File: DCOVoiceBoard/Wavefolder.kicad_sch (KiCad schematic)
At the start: 39 parts, among them Q401 BC858, Q402 BC857, Q403 BC847, Q404 BC857, Q405 BC847, U302 TMUX4053, U402 LM13700, U403 TL074

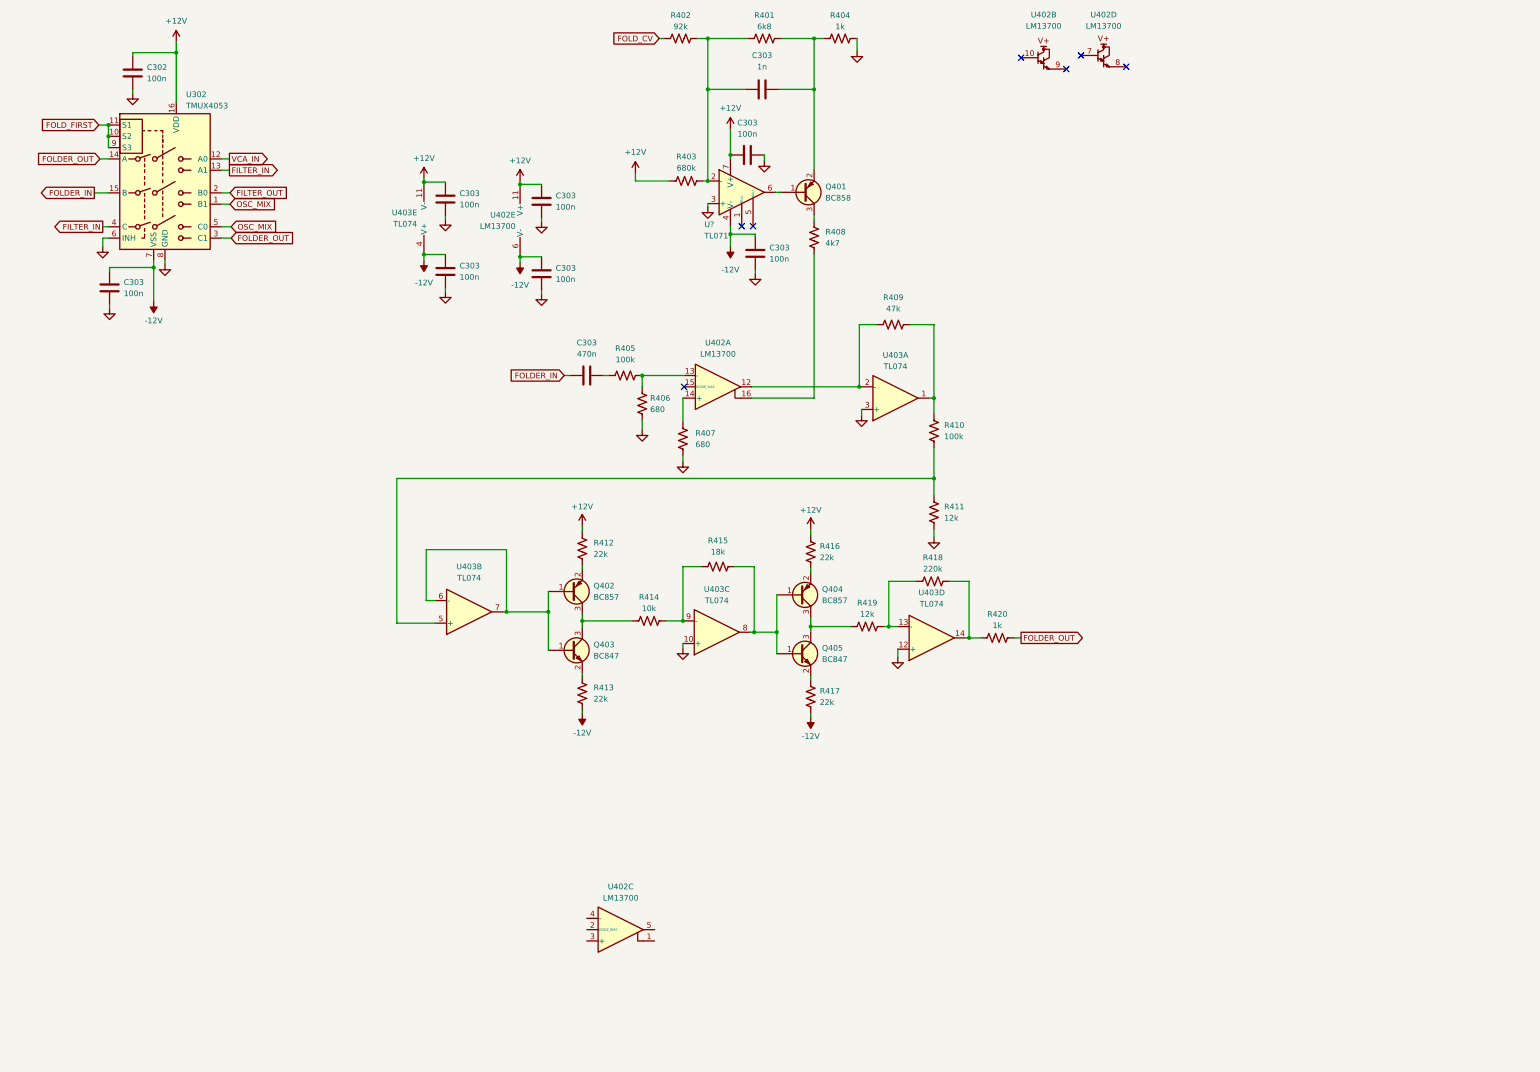
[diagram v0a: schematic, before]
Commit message: voice board rough schematic
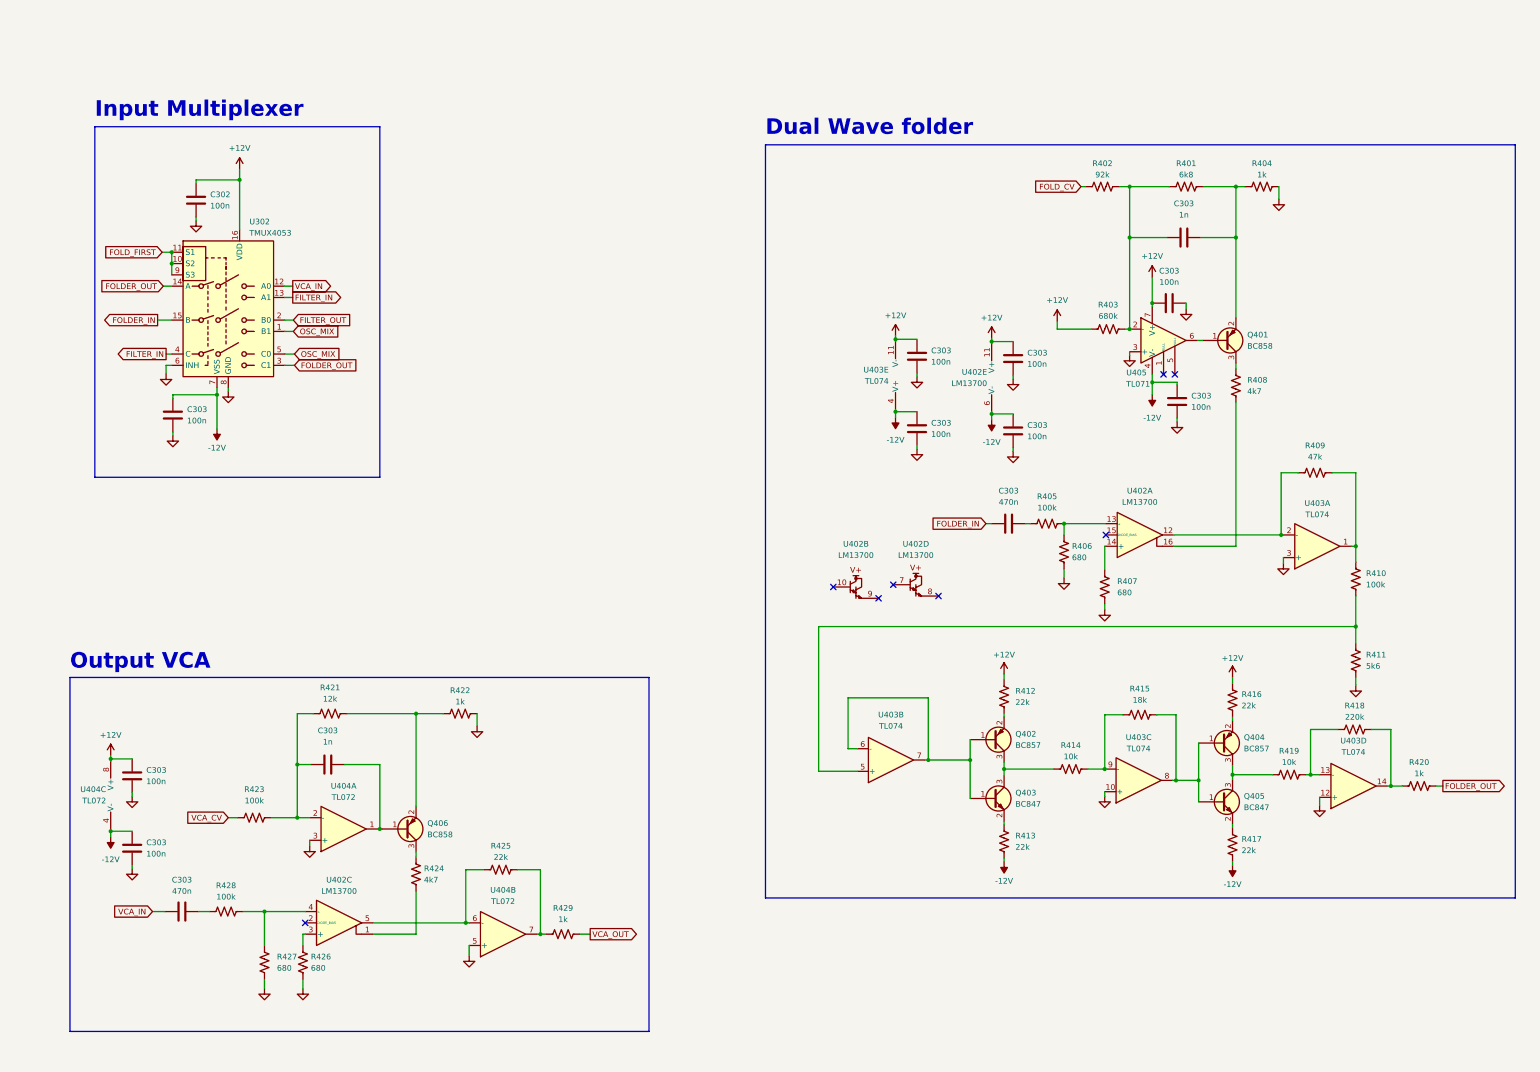
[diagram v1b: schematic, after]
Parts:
- added C303: 470n, Capacitor_SMD:C_0805_2012Metric, symbol Device:C
- added C303 (x2): 100n, Capacitor_SMD:C_0805_2012Metric, symbol Device:C
- added C303: 1n, Capacitor_SMD:C_0805_2012Metric, symbol Device:C
- added Q406: BC858, PCM_Package_TO_SOT_SMD_AKL:SOT-23, symbol PCM_Transistor_BJT_AKL:BC858
- added R421: 12k, PCM_Resistor_SMD_AKL:R_0805_2012Metric, symbol Device:R_US
- added R422, R429: 1k, PCM_Resistor_SMD_AKL:R_0805_2012Metric, symbol Device:R_US
- added R423, R428: 100k, PCM_Resistor_SMD_AKL:R_0805_2012Metric, symbol Device:R_US
- added R424: 4k7, PCM_Resistor_SMD_AKL:R_0805_2012Metric, symbol Device:R_US
- added R425: 22k, PCM_Resistor_SMD_AKL:R_0805_2012Metric, symbol Device:R_US
- added R426, R427: 680, PCM_Resistor_SMD_AKL:R_0805_2012Metric, symbol Device:R_US
- added U404: TL072, Package_SO:SOIC-8_3.9x4.9mm_P1.27mm, symbol Amplifier_Operational:TL072
- C302, C303: footprint (none) -> Capacitor_SMD:C_0805_2012Metric
- Q401, Q402, Q403, Q404, Q405: footprint Package_TO_SOT_SMD_AKL:SOT-23 -> PCM_Package_TO_SOT_SMD_AKL:SOT-23
- R401, R402, R403, R404, R405, R406, R407, R408, R409, R410, R412, R413, R414, R415, R416, R417, R418, R420: footprint (none) -> PCM_Resistor_SMD_AKL:R_0805_2012Metric
- R411: value 12k -> 5k6; footprint (none) -> PCM_Resistor_SMD_AKL:R_0805_2012Metric
- R419: value 12k -> 10k; footprint (none) -> PCM_Resistor_SMD_AKL:R_0805_2012Metric
- U302: footprint (none) -> Package_SO:TSSOP-16_4.4x5mm_P0.65mm
- U402: footprint (none) -> PCM_Package_SO_AKL:SOIC-16_3.9x9.9mm_P1.27mm
- U403: footprint (none) -> Package_SO:SOIC-14_3.9x8.7mm_P1.27mm
- U405: renamed from U?; footprint (none) -> Package_SO:SOIC-8_3.9x4.9mm_P1.27mm
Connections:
- net +12V: now also C303.1, U404.8 (V+)
- net -12V: now also C303.1, U404.4 (V-)
- net GND: now also C303.2, C303.2, R422.2, R426.1, R427.1, U404.3 (+), U404.5 (+)
- net VCA_IN: now also C303.1
- net at U402.1: now also R424.1
- net at U402.3 (+): now also R426.2
- net at U402.4 (-): now also R427.2, R428.1
- net at U402.5: now also R425.1, U404.6 (-)
- new net: C303.2, Q406.1 (B), U404.1
- new net: Q406.2 (E), R421.2, R422.1
- new net: Q406.3 (C), R424.2
- new net: R425.2, R429.1, U404.7
- new net: C303.1, R421.1, R423.2, U404.2 (-)
- new net: C303.2, R428.2
- new net VCA_CV: R423.1
- new net VCA_OUT: R429.2
- no-connect marks 7 -> 8
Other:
- note added: "Dual Wave folder"
- note added: "Input Multiplexer"
- note added: "Output VCA"
- moved on the sheet: C302, C303, Q401, Q402, Q403, Q404, Q405, R401, R402, R403, R404, R405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

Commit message: motherboard hardware
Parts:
- removed C302, C303 (x5): 100n, Capacitor_SMD:C_0805_2012Metric, symbol Device:C
- removed U302: TMUX4053, Package_SO:TSSOP-16_4.4x5mm_P0.65mm, symbol Analog_Switch:TMUX4053
- removed U404: TL072, Package_SO:SOIC-8_3.9x4.9mm_P1.27mm, symbol Amplifier_Operational:TL072
- removed U405: TL071, Package_SO:SOIC-8_3.9x4.9mm_P1.27mm, symbol Amplifier_Operational:TL071
- added C303 (x2): 100n, Capacitor_SMD:C_0805_2012Metric, symbol Device:C
- added U404: TL074, Package_SO:SOIC-14_3.9x8.7mm_P1.27mm, symbol Amplifier_Operational:TL074
- U402: footprint PCM_Package_SO_AKL:SOIC-16_3.9x9.9mm_P1.27mm -> Package_SO:SOIC-16_3.9x9.9mm_P1.27mm
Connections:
- net +12V: now also C303.1, U404.4 (V+)
- net -12V: now also C303.1, U404.11 (V-)
- net GND: now also C303.2, C303.2, U404.10 (+), U404.12 (+), U404.3 (+), U404.5 (+)
- net at C303.2, Q406.1 (B): now also U404.1
- net at C303.1, R401.1, R402.2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: now also U404.9 (-)
- net at R425.1, U402.5: now also U404.6 (-)
- net at R425.2, R429.1: now also U404.7
- net at C303.1, R421.1, R423.2: now also U404.2 (-)
- net at Q401.1 (B): now also U404.8
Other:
- note removed: "Input Multiplexer"
- moved on the sheet: C303, Q406, R421, R422, R423, R424, R425, R426, R427, R428, R429, U402C
